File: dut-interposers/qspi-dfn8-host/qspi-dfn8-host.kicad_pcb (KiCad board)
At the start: 4 copper layers, 6 x 7 mm, 3 parts, among them J1 103R010BB100, U1 W25Q80BV

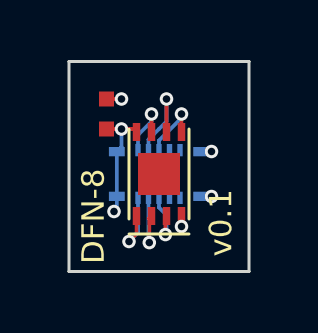
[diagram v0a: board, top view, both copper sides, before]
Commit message: added 1mm of padding to hit oshpark minimum board size
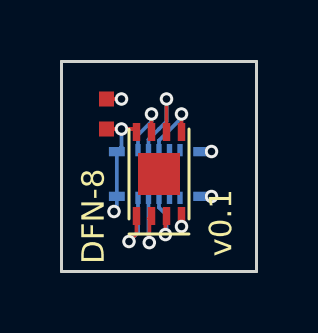
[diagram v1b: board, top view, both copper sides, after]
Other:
- board size 6 x 7 mm -> 6.5 x 7 mm
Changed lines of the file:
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@@
 	)
 	(gr_rect
-		(start 109.5 99)
-		(end 115.5 106)
+		(start 109.25 99)
+		(end 115.75 106)
 		(stroke
 			(width 0.1)
@@
 		(polygon
 			(pts
-				(xy 109.75 99.25) (xy 109.75 105.75) (xy 115.25 105.75) (xy 115.25 99.25)
+				(xy 109.5 99.25) (xy 109.5 105.75) (xy 115.5 105.75) (xy 115.5 99.25)
 			)
 		)
